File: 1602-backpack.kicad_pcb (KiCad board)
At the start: 4 copper layers, 16.3 x 42 mm, 8 parts, among them J1 Display, J2 Full, J3 Minimal

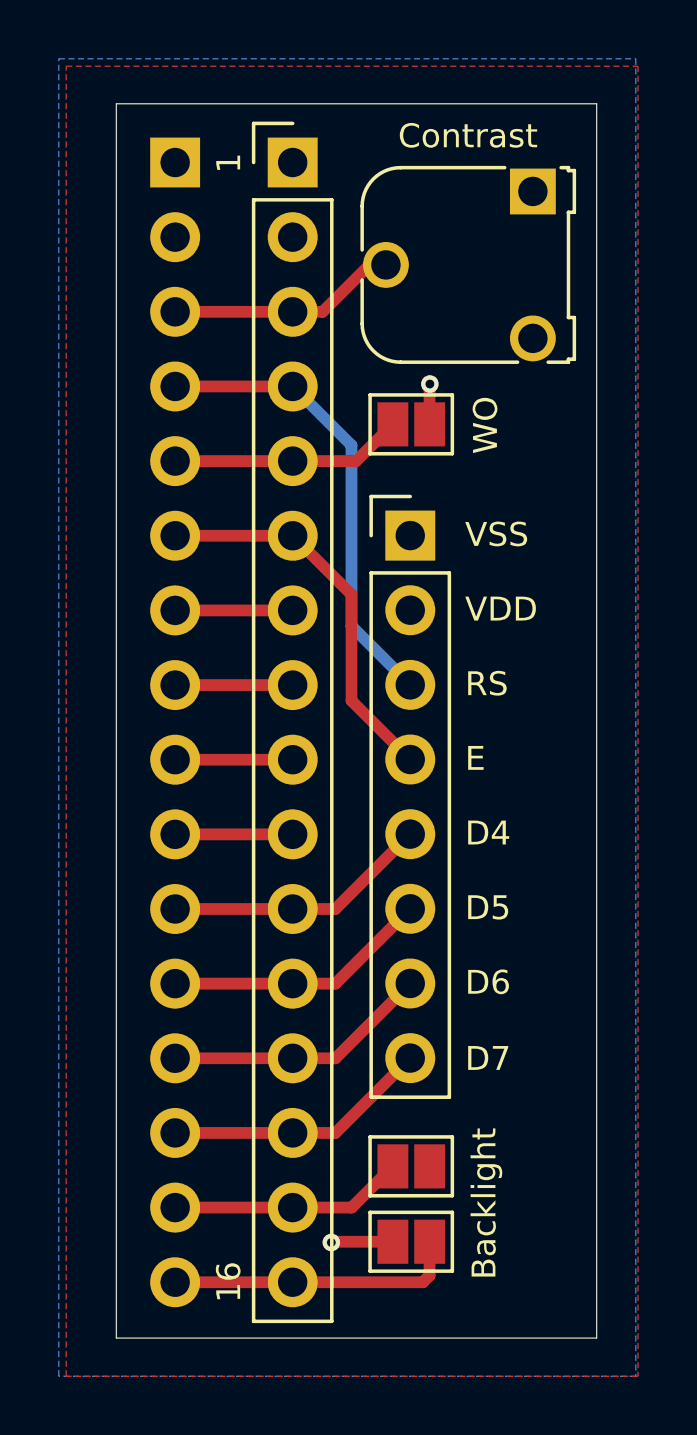
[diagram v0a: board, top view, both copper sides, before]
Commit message: Correct board
Specify order number location, remove unused copper layers, tweak size
and legend.
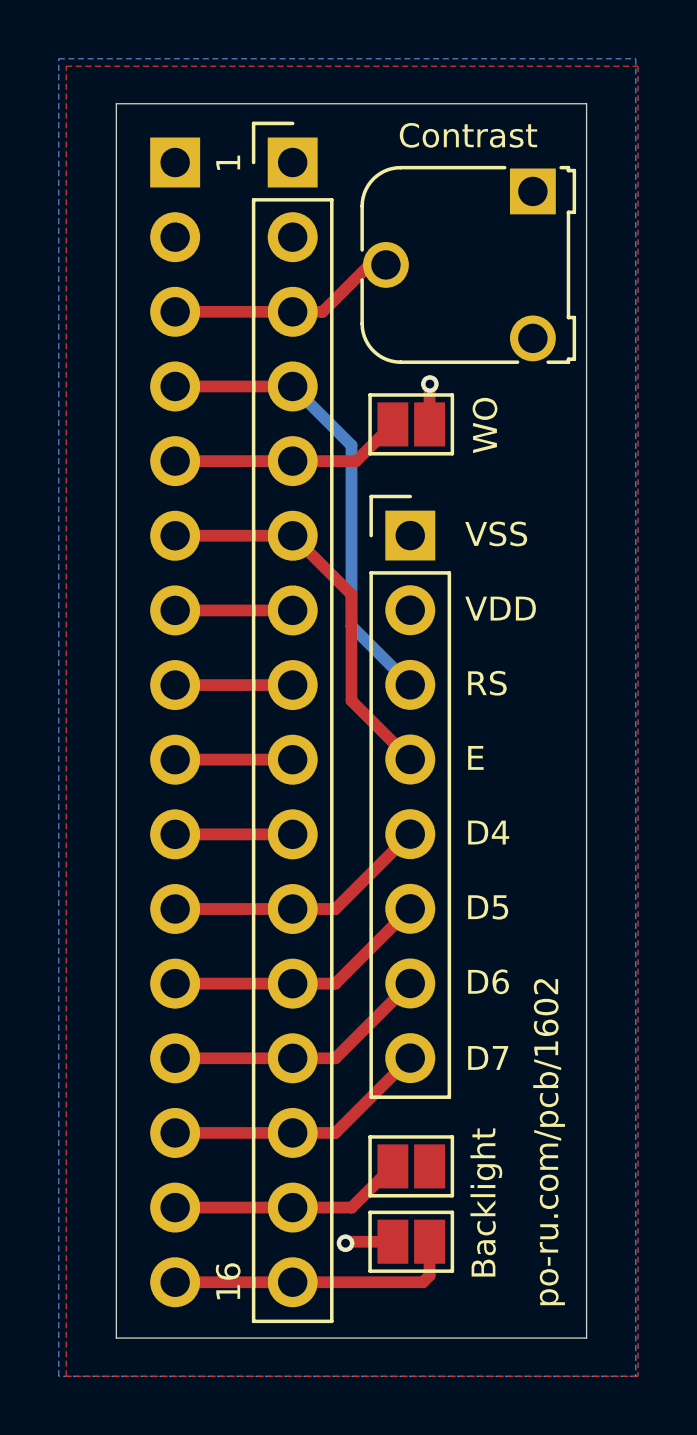
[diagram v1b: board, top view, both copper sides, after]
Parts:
- moved G*** 0.50 mm to (112.0, 88.0)
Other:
- board size 16.3 x 42 mm -> 16 x 42 mm
- copper layers 4 -> 2
- board text added: "JLCJLCJLCJLC"
- board text added: "po-ru.com/pcb/1602"
- board text removed: "1602 LCD Adapter Board Paul Battley po-ru.com/pcb/1602"

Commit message: Finalise layout and round corners
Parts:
- removed G***: LOGO, LOGO
- DS1: renamed from J1; value Display -> WC1602A
- turned JP1 to 0 degrees
- turned JP3 to 0 degrees
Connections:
- net /VDD renamed VDD
- net /VE renamed /V0
- DS1 pad 1: /VSS -> VSS
- J2 pad 1: /VSS -> VSS
- J3 pad 1: /VSS -> VSS
- JP1 pad 1: /VSS -> /RW
- JP1 pad 2: /RW -> VSS
- JP3 pad 2: /VSS -> VSS
- RV1 pad 1: /VSS -> VSS
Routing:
- net /VSS: track 3.01 -> 0.00 mm, vias 2 -> 0
- net VSS: track 0.00 -> 2.80 mm, vias 0 -> 2
- net /K: track 9.90 -> 7.98 mm
- added copper zone on B.Cu, net VSS
- removed copper zone on B.Cu, net /VSS
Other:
- outline, holes or cut-outs redrawn
- board text added: "Rev. 1 po-ru.com/pcb/1602"
- board text added: "Write only"
- board text removed: "WO"
- board text removed: "po-ru.com/pcb/1602"
